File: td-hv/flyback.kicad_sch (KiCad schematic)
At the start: 56 parts, among them Q1 BSZ42DN25NS3GATMA1, Q12 G3R450MT17J, Q2 BSZ42DN25NS3GATMA1, U1 74HC00, U13 MCP1416, U2 LM2903, U4 2ED2101S06FXUMA1

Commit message: fix some small td-hv issues
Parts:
- Q1: value BSZ42DN25NS3GATMA1 -> BSC16DN25NS3GATMA1; Digikey BSZ42DN25NS3GATMA1CT-ND -> BSC16DN25NS3GATMA1CT-ND
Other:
- note added: "todo: reconsider populated resistors"
- note removed: "todo: 24V diode too low voltage 12V feedback too high voltage switch polarity of feedback wrong MOSFET part number (too small)"
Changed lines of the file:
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@@
 		)
 	)
-	(text "todo: 24V diode too low voltage\n12V feedback too high voltage\nswitch polarity of feedback\nwrong MOSFET part number (too small)"
+	(text "todo: reconsider populated resistors"
 		(exclude_from_sim no)
 		(at 162.56 148.59 0)
@@
 			)
 		)
-		(property "Value" "BSZ42DN25NS3GATMA1"
+		(property "Value" "BSC16DN25NS3GATMA1"
 			(at 129.6416 53.213 0)
 			(effects
@@
 			)
 		)
-		(property "Digikey" "BSZ42DN25NS3GATMA1CT-ND"
+		(property "Digikey" "BSC16DN25NS3GATMA1CT-ND"
 			(at 124.46 52.07 0)
 			(effects

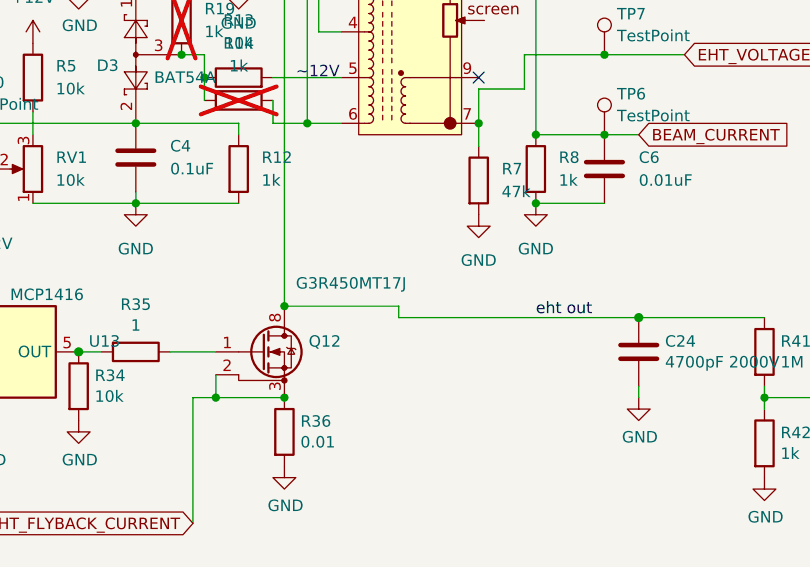
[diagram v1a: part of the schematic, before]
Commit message: swap to cheaper sic mosfet
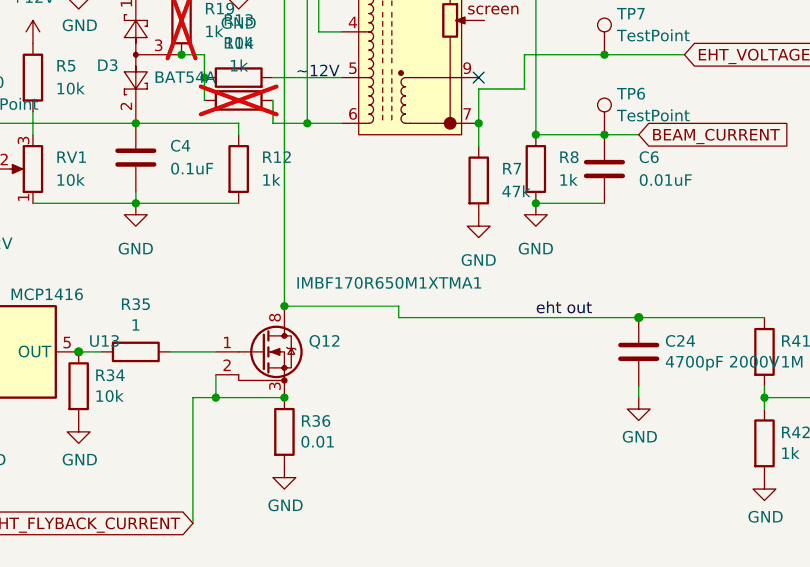
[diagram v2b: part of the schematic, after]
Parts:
- Q12: value G3R450MT17J -> IMBF170R650M1XTMA1; Digikey 1242-G3R450MT17J-ND -> 448-IMBF170R650M1XTMA1CT-ND
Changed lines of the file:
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@@
 			)
 		)
-		(property "Value" "G3R450MT17J"
+		(property "Value" "IMBF170R650M1XTMA1"
 			(at 151.13 105.41 0)
 			(effects
@@
 			)
 		)
-		(property "Datasheet" "https://genesicsemi.com/sic-mosfet/G3R450MT17J/G3R450MT17J.pdf"
+		(property "Datasheet" ""
 			(at 147.32 113.03 0)
 			(effects
@@
 			)
 		)
-		(property "Digikey" "1242-G3R450MT17J-ND"
+		(property "Digikey" "448-IMBF170R650M1XTMA1CT-ND"
 			(at 147.32 113.03 0)
 			(effects

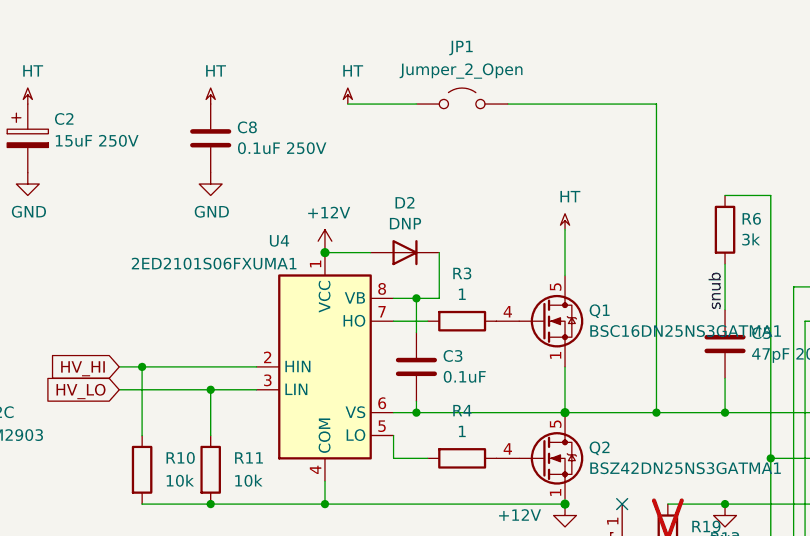
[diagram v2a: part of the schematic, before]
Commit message: swap to cheaper capacitor
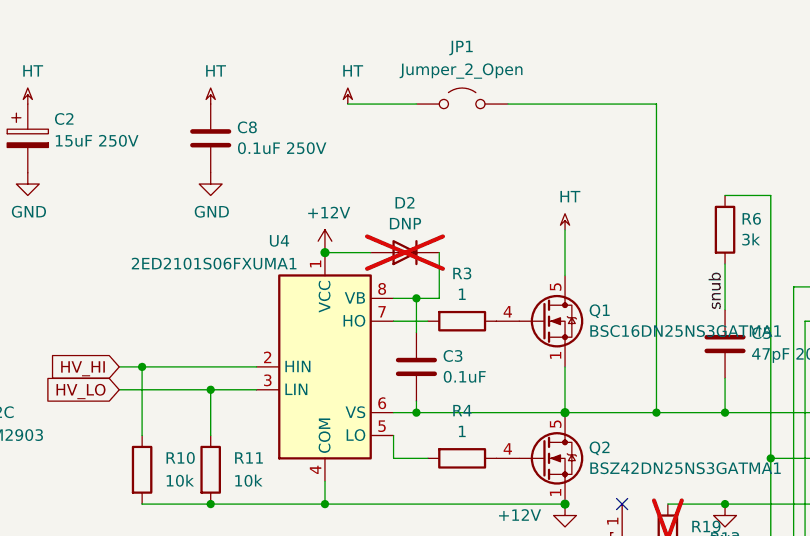
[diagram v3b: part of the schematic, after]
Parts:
- C5: Digikey 478-4734-1-ND -> 478-KGM43BCG3U470JVCT-ND
- D2: now not fitted; now left out of the parts list
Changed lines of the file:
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@@
 		(unit 1)
 		(exclude_from_sim no)
-		(in_bom yes)
+		(in_bom no)
 		(on_board yes)
-		(dnp no)
+		(dnp yes)
 		(property "Reference" "D2"
 			(at 109.22 38.9636 0)
@@
 			)
 		)
-		(property "Digikey" "478-4734-1-ND"
+		(property "Digikey" "478-KGM43BCG3U470JVCT-ND"
 			(at 144.78 54.61 0)
 			(effects
